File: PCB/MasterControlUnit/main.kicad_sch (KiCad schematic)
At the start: 6 parts, among them U1 STM32F407G-DISC1, U15 MCP23017_SO, U5 LD1117S33TR_SOT223

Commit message: Analog input protection added
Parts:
- added C1, C2: 10nF, Capacitor_THT:CP_Radial_D6.3mm_P2.50mm, symbol Device:C
- added J3: An-IN, Connector_PinHeader_2.54mm:PinHeader_1x03_P2.54mm_Vertical, symbol Connector_Generic:Conn_01x03
- added R2, R3: 4.7K, Resistor_SMD:R_1206_3216Metric, symbol Device:R
- added R4, R5: 12K, Resistor_SMD:R_1206_3216Metric, symbol Device:R
- added R6, R7: 1K, Resistor_SMD:R_1206_3216Metric, symbol Device:R
- added R8, R9: 22K, Resistor_SMD:R_1206_3216Metric, symbol Device:R
- added U17: ADA4096-2ARMZ, ADA4096-2ARMZ:RM_8_ADI, symbol ADA4096-2ARMZ:ADA4096-2ARMZ
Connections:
- net +3.3V: now also R2.1, R3.1, U17.8 (V+)
- net GND: now also C1.1, C2.1, J3.1 (Pin_1), R8.1, R9.1, U17.4 (V-)
- net I2C1_SCL ESP32: now also R3.2
- net I2C1_SDA ESP32: now also R2.2
- net ADC_1: no longer names the net of U1.P1_8 (PC0)
- net ADC_1: now also R6.1
- net ADC_2: no longer names the net of U1.P1_7 (PC1)
- net ADC_2: now also R7.1
- new net: C2.2, R4.1, R9.2, U17.3 (INA+)
- new net: R6.2, U17.1 (OUTA), U17.2 (INA-)
- new net: C1.2, R5.1, R8.2, U17.5 (INB+)
- new net: R7.2, U17.6 (INB-), U17.7 (OUTB)
- new net: J3.2 (Pin_2), R5.2
- new net: J3.3 (Pin_3), R4.2

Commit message: ISRAM SPI not connected to the engine fixed
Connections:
- net MISO is gone; now on net MISO from ISRAM: U1.P1_38 (PB14)
- net MOSI is gone; now on net MOSI to ISRAM: U1.P1_39 (PB15)
- net SCL/SCK is gone; now on net SCL/SCK to ISRAM: U1.P1_37 (PB13)
- net ISRAM ADDR 0: now also U1.P1_36 (PB12)
- net OSRAM B-EN: no longer U1.P2_32 (PD4)
- net CS renamed ISRAM B-EN
- net ISRAM B-EN: now also U1.P2_32 (PD4)

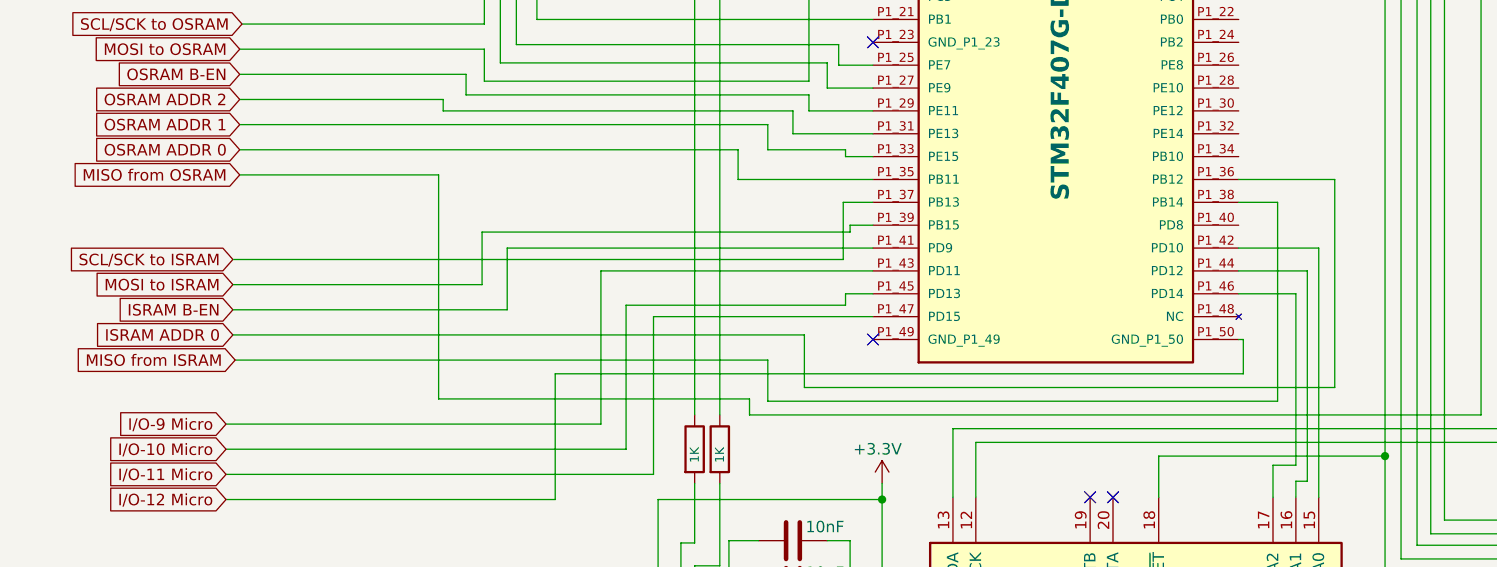
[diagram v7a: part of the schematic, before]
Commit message: Wrong label and unconnected pin fixed
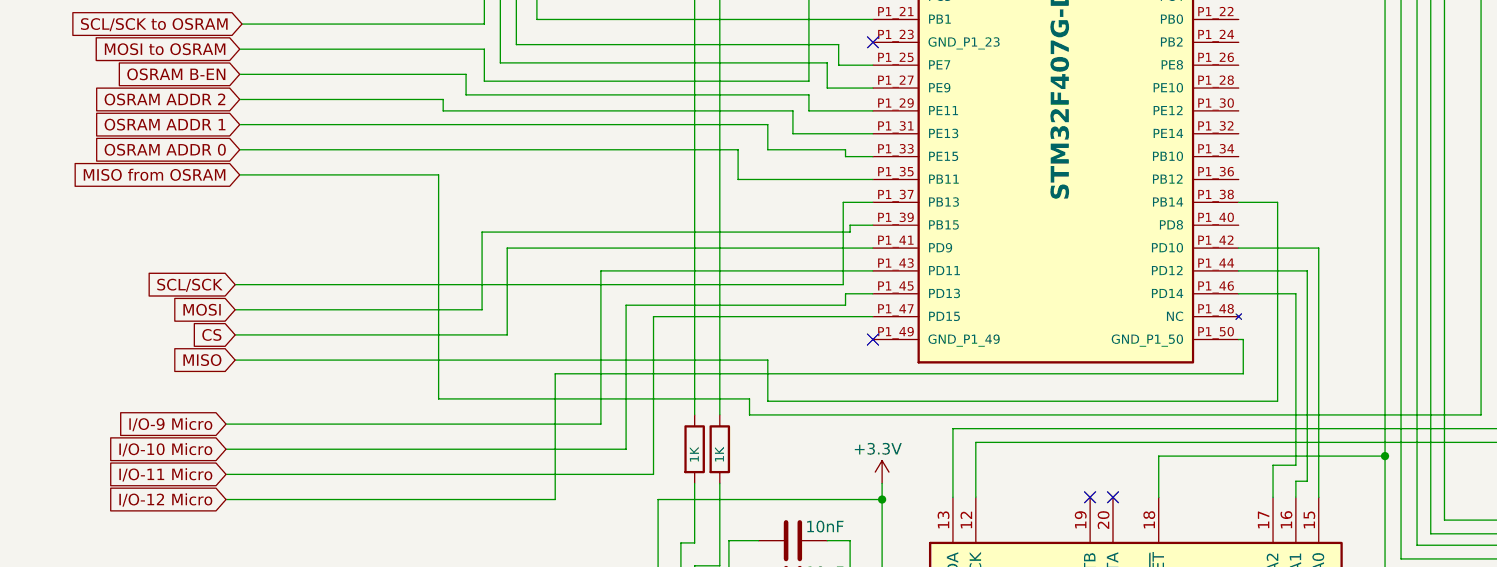
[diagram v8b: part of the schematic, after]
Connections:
- net ISRAM ADDR 0: no longer U1.P1_36 (PB12)
- net ISRAM B-EN: no longer U1.P1_41 (PD9)
- net MISO from ISRAM: no longer U1.P1_38 (PB14)
- net MOSI to ISRAM: no longer U1.P1_39 (PB15)
- net SCL/SCK to ISRAM: no longer U1.P1_37 (PB13)
- new net CS: U1.P1_41 (PD9)
- new net MISO: U1.P1_38 (PB14)
- new net MOSI: U1.P1_39 (PB15)
- new net SCL/SCK: U1.P1_37 (PB13)
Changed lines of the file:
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@@
 	(wire
 		(pts
-			(xy 163.576 134.366) (xy 163.576 111.252)
-		)
-		(stroke
-			(width 0)
-			(type default)
-		)
-	)
-	(wire
-		(pts
 			(xy 160.528 121.412) (xy 160.528 144.78)
 		)
@@
 	(wire
 		(pts
-			(xy 163.576 111.252) (xy 152.908 111.252)
-		)
-		(stroke
-			(width 0)
-			(type default)
-		)
-	)
-	(wire
-		(pts
 			(xy 112.268 116.332) (xy 109.728 116.332)
 		)
@@
 	(wire
 		(pts
-			(xy 108.966 120.142) (xy 108.966 113.792)
+			(xy 108.966 122.936) (xy 108.966 113.792)
 		)
 		(stroke
@@
 	(wire
 		(pts
-			(xy 41.148 122.936) (xy 68.834 122.936)
+			(xy 41.402 125.73) (xy 68.834 125.73)
 		)
 		(stroke
@@
 	(wire
 		(pts
-			(xy 68.834 117.094) (xy 68.834 122.936)
+			(xy 68.834 117.094) (xy 68.834 125.73)
 		)
 		(stroke
@@
 	(wire
 		(pts
-			(xy 41.148 120.142) (xy 108.966 120.142)
+			(xy 41.402 122.936) (xy 108.966 122.936)
 		)
 		(stroke
@@
 	(wire
 		(pts
-			(xy 104.648 134.366) (xy 163.576 134.366)
-		)
-		(stroke
-			(width 0)
-			(type default)
-		)
-	)
-	(wire
-		(pts
 			(xy 267.716 94.488) (xy 246.38 94.488)
 		)
@@
 	(wire
 		(pts
-			(xy 104.648 128.524) (xy 104.648 134.366)
-		)
-		(stroke
-			(width 0)
-			(type default)
-		)
-	)
-	(wire
-		(pts
 			(xy 42.164 78.232) (xy 77.47 78.232)
 		)
@@
 	(wire
 		(pts
-			(xy 41.148 128.524) (xy 104.648 128.524)
-		)
-		(stroke
-			(width 0)
-			(type default)
-		)
-	)
-	(wire
-		(pts
 			(xy 144.018 141.986) (xy 144.018 146.558)
 		)
@@
 	(wire
 		(pts
-			(xy 41.148 125.73) (xy 71.628 125.73)
+			(xy 41.402 128.524) (xy 71.628 128.524)
 		)
 		(stroke
@@
 	(wire
 		(pts
-			(xy 71.628 118.872) (xy 71.628 125.73)
+			(xy 71.628 118.872) (xy 71.628 128.524)
 		)
 		(stroke
@@
 		)
 	)
-	(global_label "SCL{slash}SCK to ISRAM"
+	(global_label "SCL{slash}SCK"
 		(shape input)
-		(at 41.148 120.142 180)
+		(at 41.402 122.936 180)
 		(fields_autoplaced yes)
 		(effects
 			(font
 				(size 1.27 1.27)
+				(color 0 72 0 1)
 			)
 			(justify right)
 		)
 		(property "Intersheetrefs" "${INTERSHEET_REFS}"
-			(at 20.141 120.142 0)
+			(at 29.8292 122.936 0)
 			(effects
 				(font
@@
 		)
 	)
-	(global_label "MISO from ISRAM"
+	(global_label "MISO"
 		(shape input)
 		(at 41.402 131.318 180)
@@
 			(font
 				(size 1.27 1.27)
+				(color 0 72 0 1)
 			)
 			(justify right)
 		)
 		(property "Intersheetrefs" "${INTERSHEET_REFS}"
-			(at 21.9069 131.318 0)
+			(at 33.8206 131.318 0)
 			(effects
 				(font
@@
 		)
 	)
-	(global_label "ISRAM ADDR 0"
-		(shape input)
-		(at 41.148 128.524 180)
-		(fields_autoplaced yes)
-		(effects
-			(font
-				(size 1.27 1.27)
-			)
-			(justify right)
-		)
-		(property "Intersheetrefs" "${INTERSHEET_REFS}"
-			(at 24.4952 128.524 0)
-			(effects
-				(font
-					(size 1.27 1.27)
-				)
-				(justify right)
-				(hide yes)
-			)
-		)
-	)
 	(global_label "PWM_1"
 		(shape input)
@@
 		)
 	)
-	(global_label "ISRAM B-EN"
+	(global_label "CS"
 		(shape input)
-		(at 41.148 125.73 180)
+		(at 41.402 128.524 180)
 		(fields_autoplaced yes)
 		(effects
 			(font
 				(size 1.27 1.27)
+				(color 0 72 0 1)
 			)
 			(justify right)
 		)
 		(property "Intersheetrefs" "${INTERSHEET_REFS}"
-			(at 26.249 125.73 0)
+			(at 35.9373 128.524 0)
 			(effects
 				(font
@@
 		)
 	)
-	(global_label "MOSI to ISRAM"
+	(global_label "MOSI"
 		(shape input)
-		(at 41.148 122.936 180)
+		(at 41.402 125.73 180)
 		(fields_autoplaced yes)
 		(effects
 			(font
 				(size 1.27 1.27)
+				(color 0 72 0 1)
 			)
 			(justify right)
 		)
 		(property "Intersheetrefs" "${INTERSHEET_REFS}"
-			(at 24.1324 122.936 0)
+			(at 33.8206 125.73 0)
 			(effects
 				(font
